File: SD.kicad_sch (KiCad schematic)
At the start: 4 parts, among them J5 Micro_SD_Card_Det2

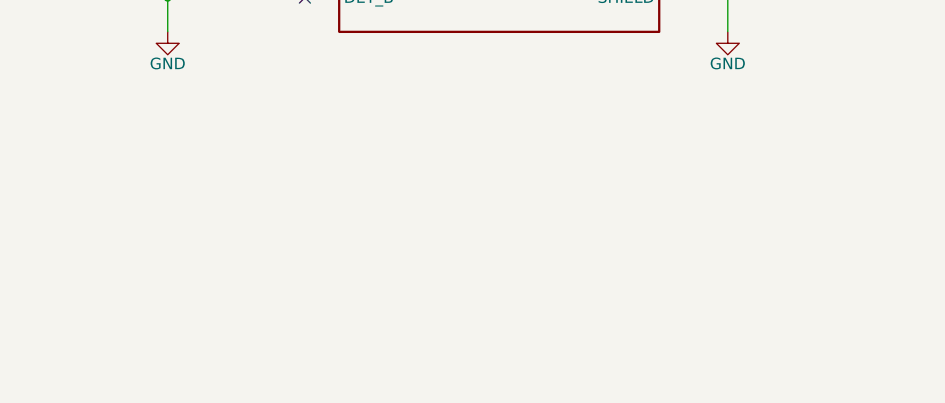
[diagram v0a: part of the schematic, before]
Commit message: Added better protection to SD card, Jetson IO, and added address breakouts to power monitors
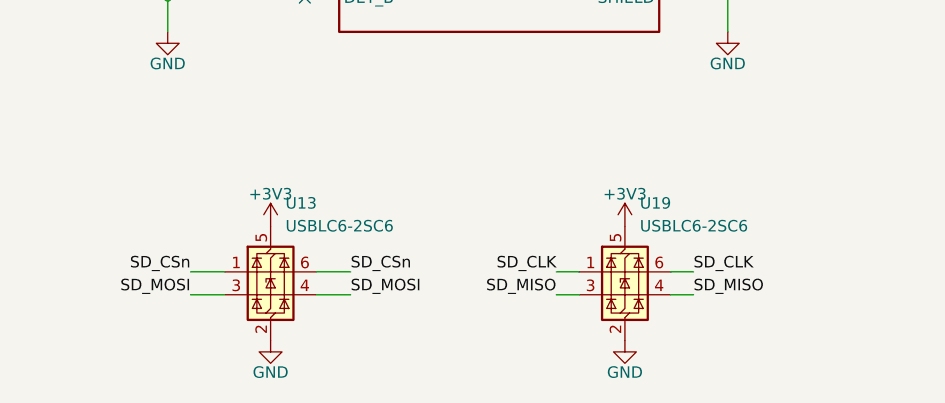
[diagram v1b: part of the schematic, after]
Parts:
- added U13, U19: USBLC6-2SC6, Package_TO_SOT_SMD:SOT-23-6, symbol Power_Protection:USBLC6-2SC6
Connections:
- net +3V3: now also U13.5 (VBUS), U19.5 (VBUS)
- net CSn: now also U13.1 (I/O1), U13.6 (I/O1)
- net GND: now also U13.2 (GND), U19.2 (GND)
- net SD_CLK: now also U19.1 (I/O1), U19.6 (I/O1)
- net SD_MISO: now also U19.3 (I/O2), U19.4 (I/O2)
- net SD_MOSI: now also U13.3 (I/O2), U13.4 (I/O2)

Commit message: Updated version to v2.1
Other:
- company: (none) -> Carnegie Mellon University
- title: (none) -> Argus Mainboard
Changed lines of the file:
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@@
 	(generator_version "8.0")
 	(paper "A4")
+	(title_block
+		(title "Argus Mainboard")
+		(date "2024-11-19")
+		(rev "v2.1")
+		(company "Carnegie Mellon University")
+		(comment 1 "M. Holliday")
+		(comment 2 "N. Khera")
+		(comment 3 "V. Rajesh")
+	)
 	(junction
 		(at 71.12 105.41)

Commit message: v3 partial schematic updates
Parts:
- removed U13, U19: USBLC6-2SC6, Package_TO_SOT_SMD:SOT-23-6, symbol Power_Protection:USBLC6-2SC6
- added F1: 500mA, symbol Device:Fuse_Small
- J5: value Micro_SD_Card_Det2 -> 104031-0811
- R48: value 10K -> 10k
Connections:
- net +3V3 renamed +3V3_SD
- net +3V3_SD: now also F1.2
- new net +3V3_P: F1.1
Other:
- moved on the sheet: C32, C33, J5, R48

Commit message: v3 Layout complete
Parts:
- F1: footprint (none) -> Fuse:Fuse_0603_1608Metric
- renumbered C32 to C72, C33 to C73, J5 to J4, R48 to R128
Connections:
- net CSn renamed SD_CSn
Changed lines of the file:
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@@
 	(title_block
 		(title "Argus Mainboard")
-		(date "2024-11-19")
-		(rev "v2.1")
+		(date "2025-01-08")
+		(rev "v3.0")
 		(company "Carnegie Mellon University")
 		(comment 1 "M. Holliday")
@@
 	(label "SD_MISO"
 		(at 74.93 105.41 0)
-		(fields_autoplaced yes)
 		(effects
 			(font
@@
 	(label "MISO"
 		(at 215.9 107.95 0)
-		(fields_autoplaced yes)
 		(effects
 			(font
@@
 	(label "SD_CSn"
 		(at 74.93 92.71 0)
-		(fields_autoplaced yes)
 		(effects
 			(font
@@
 	(label "SD_MOSI"
 		(at 163.83 104.14 0)
-		(fields_autoplaced yes)
 		(effects
 			(font
@@
 	(label "SD_CLK"
 		(at 74.93 100.33 0)
-		(fields_autoplaced yes)
 		(effects
 			(font
@@
 	(label "SD_CSn"
 		(at 215.9 96.52 0)
-		(fields_autoplaced yes)
 		(effects
 			(font
@@
 	(label "SD_MISO"
 		(at 163.83 107.95 0)
-		(fields_autoplaced yes)
 		(effects
 			(font
@@
 	(label "CLK"
 		(at 215.9 100.33 0)
-		(fields_autoplaced yes)
 		(effects
 			(font
@@
 	(label "SD_MOSI"
 		(at 74.93 95.25 0)
-		(fields_autoplaced yes)
 		(effects
 			(font
@@
 	(label "MOSI"
 		(at 215.9 104.14 0)
-		(fields_autoplaced yes)
 		(effects
 			(font
@@
 	(label "SD_CLK"
 		(at 163.83 100.33 0)
-		(fields_autoplaced yes)
 		(effects
 			(font
@@
 		(shape input)
 		(at 226.06 104.14 0)
-		(fields_autoplaced yes)
 		(effects
 			(font
@@
 		(shape input)
 		(at 226.06 100.33 0)
-		(fields_autoplaced yes)
 		(effects
 			(font
@@
 		(shape output)
 		(at 226.06 107.95 0)
-		(fields_autoplaced yes)
 		(effects
 			(font
@@
 		)
 	)
-	(hierarchical_label "CSn"
+	(hierarchical_label "SD_CSn"
 		(shape input)
 		(at 226.06 96.52 0)
-		(fields_autoplaced yes)
 		(effects
 			(font
@@
 		(on_board yes)
 		(dnp no)
-		(property "Reference" "C32"
+		(property "Reference" "C72"
 			(at 60.198 99.314 0)
 			(effects
@@
 			(project "Avionics-MainBoard"
 				(path "/4c932743-8c6f-426e-9c1f-5a3f2b32c70d/00f4ddfb-afd6-4184-9f71-0fb73daba661"
-					(reference "C32")
+					(reference "C72")
 					(unit 1)
 				)
@@
 		(on_board yes)
 		(dnp no)
-		(property "Reference" "R48"
+		(property "Reference" "R128"
 			(at 80.01 83.82 90)
 			(effects
@@
 			(project "Avionics-MainBoard"
 				(path "/4c932743-8c6f-426e-9c1f-5a3f2b32c70d/00f4ddfb-afd6-4184-9f71-0fb73daba661"
-					(reference "R48")
+					(reference "R128")
 					(unit 1)
 				)
@@
 		(on_board yes)
 		(dnp no)
-		(property "Reference" "C33"
+		(property "Reference" "C73"
 			(at 69.088 99.314 0)
 			(effects
@@
 			(project "Avionics-MainBoard"
 				(path "/4c932743-8c6f-426e-9c1f-5a3f2b32c70d/00f4ddfb-afd6-4184-9f71-0fb73daba661"
-					(reference "C33")
+					(reference "C73")
 					(unit 1)
 				)
@@
 		(on_board yes)
 		(dnp no)
-		(fields_autoplaced yes)
-		(property "Reference" "J5"
-			(at 111.125 78.74 0)
+		(property "Reference" "J4"
+			(at 110.49 80.264 0)
 			(effects
 				(font
@@
 		)
 		(property "Value" "104031-0811"
-			(at 111.125 81.28 0)
+			(at 110.49 82.296 0)
 			(effects
 				(font
@@
 			(project "Avionics-MainBoard"
 				(path "/4c932743-8c6f-426e-9c1f-5a3f2b32c70d/00f4ddfb-afd6-4184-9f71-0fb73daba661"
-					(reference "J5")
+					(reference "J4")
 					(unit 1)
 				)
@@
 			)
 		)
-		(property "Footprint" ""
+		(property "Footprint" "Fuse:Fuse_0603_1608Metric"
 			(at 54.61 87.63 0)
 			(effects

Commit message: v4.0 Updates
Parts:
- renumbered C72 to C70, C73 to C71, R128 to R118
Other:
- sheet SPI Protection renamed SPI Protection1
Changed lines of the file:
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@@
 (kicad_sch
-	(version 20231120)
+	(version 20250114)
 	(generator "eeschema")
-	(generator_version "8.0")
+	(generator_version "9.0")
 	(paper "A4")
 	(title_block
@@
 		(comment 3 "V. Rajesh")
 	)
+	(text "MicroSD Card"
+		(exclude_from_sim no)
+		(at 100.076 75.946 0)
+		(effects
+			(font
+				(size 2.159 2.159)
+			)
+			(justify left bottom)
+		)
+	)
 	(junction
 		(at 71.12 102.87)
@@
 			(width 0)
 			(type default)
-		)
-	)
-	(text "MicroSD Card"
-		(exclude_from_sim no)
-		(at 100.076 75.946 0)
-		(effects
-			(font
-				(size 2.159 2.159)
-			)
-			(justify left bottom)
 		)
 	)
@@
 		(on_board yes)
 		(dnp no)
-		(property "Reference" "C72"
+		(property "Reference" "C70"
 			(at 60.198 99.314 0)
 			(effects
@@
 			(project "Avionics-MainBoard"
 				(path "/4c932743-8c6f-426e-9c1f-5a3f2b32c70d/00f4ddfb-afd6-4184-9f71-0fb73daba661"
-					(reference "C72")
+					(reference "C70")
 					(unit 1)
 				)
@@
 		(on_board yes)
 		(dnp no)
-		(property "Reference" "R128"
+		(property "Reference" "R118"
 			(at 80.01 83.82 90)
 			(effects
@@
 			(project "Avionics-MainBoard"
 				(path "/4c932743-8c6f-426e-9c1f-5a3f2b32c70d/00f4ddfb-afd6-4184-9f71-0fb73daba661"
-					(reference "R128")
+					(reference "R118")
 					(unit 1)
 				)
@@
 		(on_board yes)
 		(dnp no)
-		(property "Reference" "C73"
+		(property "Reference" "C71"
 			(at 69.088 99.314 0)
 			(effects
@@
 			(project "Avionics-MainBoard"
 				(path "/4c932743-8c6f-426e-9c1f-5a3f2b32c70d/00f4ddfb-afd6-4184-9f71-0fb73daba661"
-					(reference "C73")
+					(reference "C71")
 					(unit 1)
 				)
@@
 		(at 175.26 93.98)
 		(size 38.1 16.51)
+		(exclude_from_sim no)
+		(in_bom yes)
+		(on_board yes)
+		(dnp no)
 		(fields_autoplaced yes)
 		(stroke
@@
 			(color 0 0 0 0.0000)
 		)
-		(property "Sheetname" "SPI Protection"
+		(property "Sheetname" "SPI Protection1"
 			(at 175.26 93.2684 0)
 			(effects

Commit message: DFM updates
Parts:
- C71: MPN (none) -> C307348
- J4: MPN (none) -> C585350
- R118: MPN (none) -> C2479067
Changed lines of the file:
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@@
+			)
+		)
+		(property "MPN" "C2479067"
+			(at 80.01 87.63 90)
+			(effects
+				(font
+					(size 1.27 1.27)
+				)
+				(hide yes)
 			)
 		)
@@
 			)
 		)
+		(property "MPN" "C307348"
+			(at 71.12 100.33 0)
+			(effects
+				(font
+					(size 1.27 1.27)
+				)
+				(hide yes)
+			)
+		)
 		(pin "1"
 		)
@@
 			(at 110.49 100.33 0)
 			(effects
+				(font
+					(size 1.27 1.27)
+				)
+				(hide yes)
+			)
+		)
+		(property "MPN" "C585350"
+			(at 110.49 100.33 0)
+			(effects
